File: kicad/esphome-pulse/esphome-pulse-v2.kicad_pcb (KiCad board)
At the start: 2 copper layers, 26.3 x 24.7 mm, 3 parts, among them U2 PJ-320A

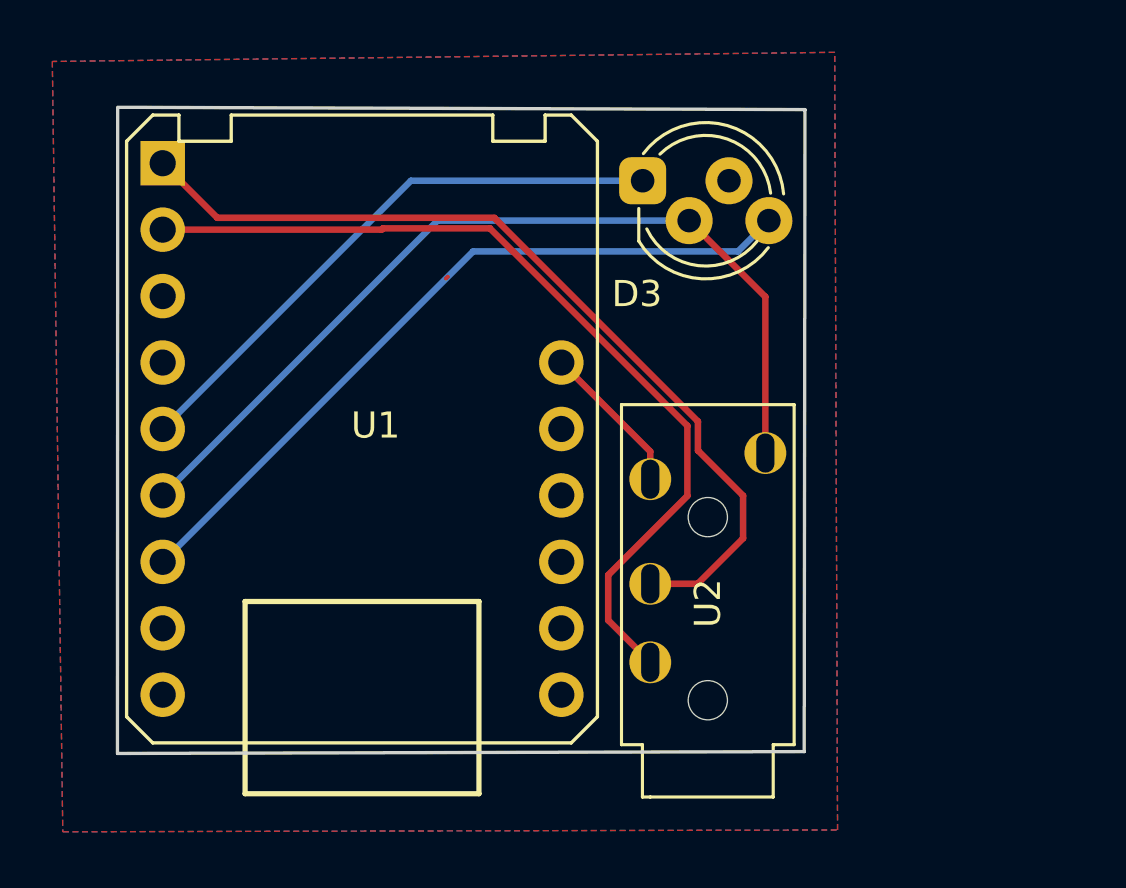
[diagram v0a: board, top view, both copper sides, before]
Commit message: Add second version of PCB with smaller barrel jack
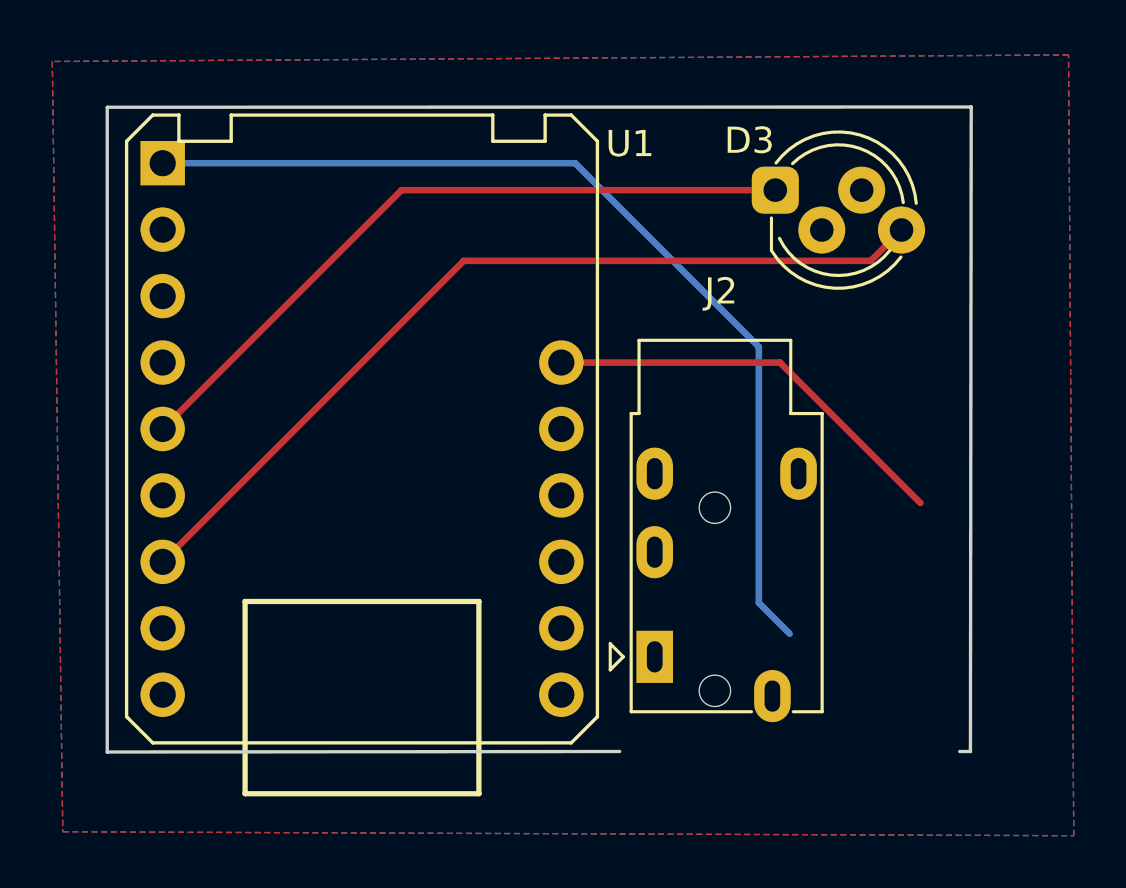
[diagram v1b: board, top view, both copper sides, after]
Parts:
- removed U2: PJ-320A, nathanhborger-PJ-320A:PJ-320A
- added J2: AudioJack2, Connector_Audio:Jack_3.5mm_PJ320E_Horizontal, F.Cu at (89.9, 89.7)
- moved D3 5.08 mm to (94.5, 71.8)
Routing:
- net GND: track 34.6 -> 0.00 mm
- net unconnected-(U1-A1CH2/TCH3/GPIO3-Pad3): track 34.2 -> 0.00 mm
- net +3.3V: track 5.87 -> 16.0 mm
- net Net-(D3-DIN): track 22.3 -> 27.2 mm
- net +5V: track 28.9 -> 33.8 mm
- net Net-(U1-A1CH0/TCH1/GPIO1): track 34.0 -> 37.2 mm
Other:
- board size 26.3 x 24.7 mm -> 33 x 24.7 mm
- board text added: "openenergy.com.au esphome-pulse April 2025 v1.0"
